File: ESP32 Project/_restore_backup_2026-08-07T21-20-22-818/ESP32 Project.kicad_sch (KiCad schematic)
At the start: 25 parts, among them J1 2338792-1, J2 B2B-PH-SM4-TB, U1 MCP73871

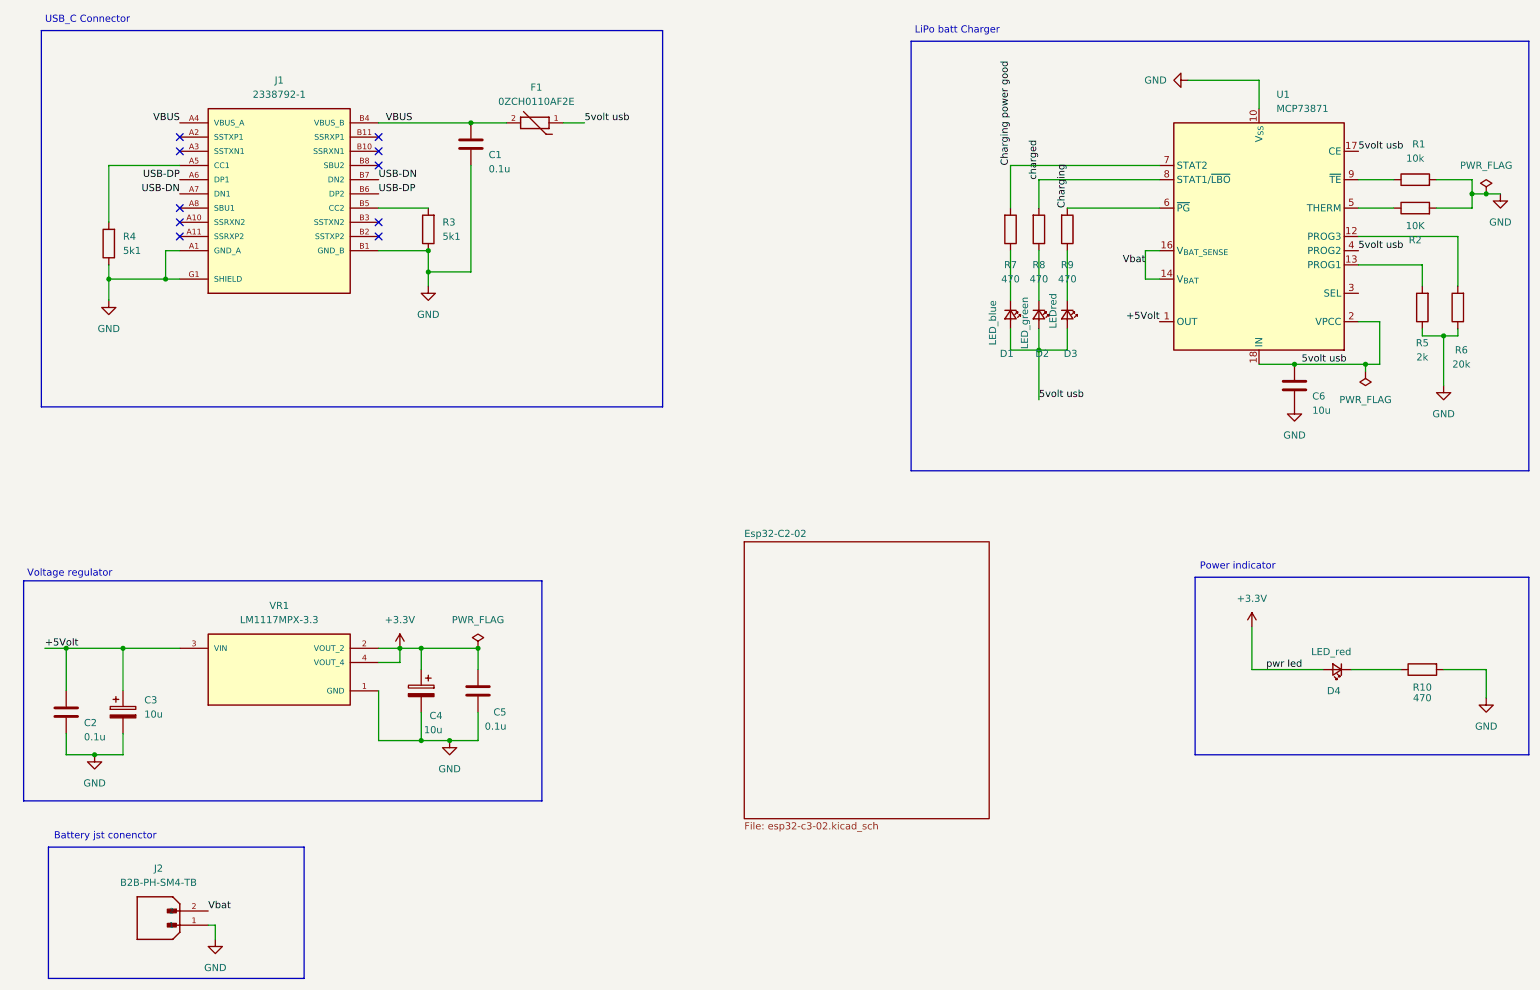
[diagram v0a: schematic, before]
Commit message: esp 32 symbols and footprint got edit and more work have done
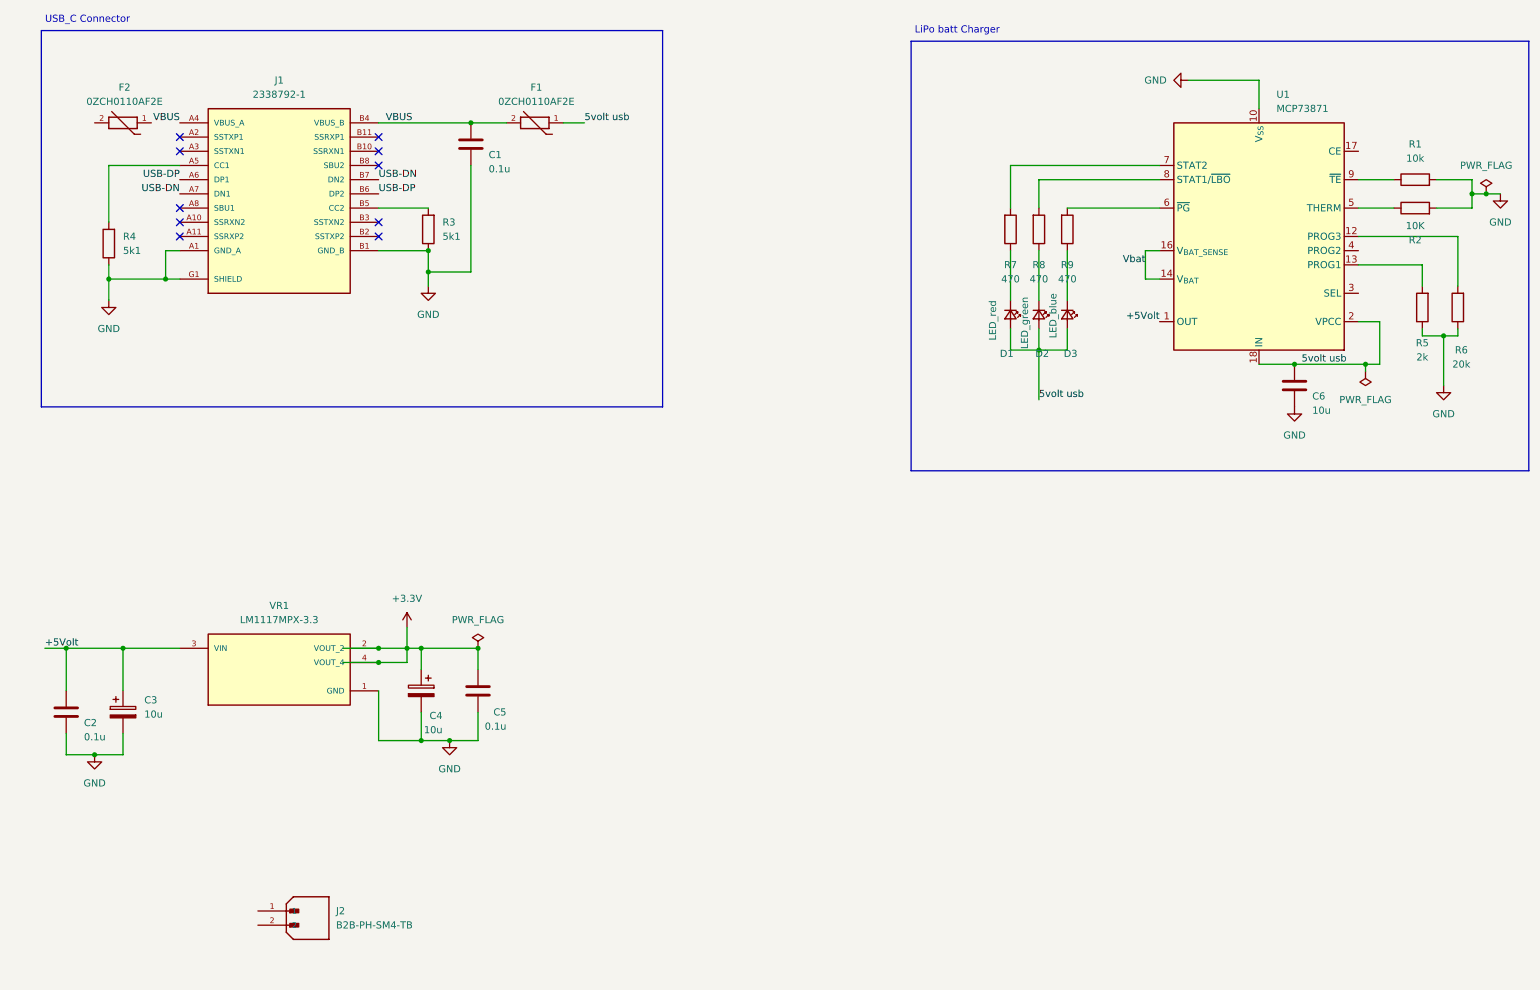
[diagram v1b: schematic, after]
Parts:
- removed D4: LED_red, LED_SMD:LED_0805_2012Metric_Pad1.15x1.40mm_HandSolder, symbol Device:LED_Small
- removed R10: 470, symbol Device:R
- added F2: 0ZCH0110AF2E, 0ZCH0110AF2E:FUSC3225X100N, symbol 0ZCH0110AF2E:0ZCH0110AF2E
- D1: value LED_blue -> LED_red
- D3: value LEDred -> LED_blue
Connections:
- net 5volt usb: no longer U1.17 (CE), U1.4 (PROG2)
- net GND: no longer J2.1
- net Vbat: no longer J2.2
- net Charging: no longer names the net of R9.2, U1.6 (~{PG})
- net Charging power good: no longer names the net of R7.2, U1.7 (STAT2)
- net charged: no longer names the net of R8.2, U1.8 (STAT1/~{LBO})
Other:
- removed sheet Esp32-C2-02
- note removed: "Battery jst conenctor"
- note removed: "Power indicator"
- note removed: "Voltage regulator"
- moved on the sheet: J2
